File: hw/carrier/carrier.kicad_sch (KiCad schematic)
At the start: 50 parts, among them J2 PCM5102A I2S, J3 PCM5102A analog, J4 MAX4466 pigtail, J5 TP4056 OUT-/B-, J6 TP4056 B+/OUT+, J7 debug TX, J8 LiPo JST-PH, J9 TP4056 IN+ wire (J6b), Q1 DMG3415U, Q2 BC557, SW1 power SPDT 1A, SW2 MODE 6x6, U1 TL431, X1 scope X RCA pads, Y1 scope Y RCA pads

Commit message: hw+docs: apply the 2026-07-26 power-path design review
Multi-agent adversarial review of the carrier's §4 load-sharing power path
(docs/hardware/pcb-review-findings.md, added here) found the TL431 trip
point mis-derived and several safety-critical instructions wrong.  This
applies the fixes and reconciles every document that repeated them.

BOM / netlist (design.py is the source of truth; board + schematic regenerated):
  - R7 75k -> 8.2k, R8 10k, R9 2.2k -> 1k.  The old derivation dropped the
    TL431 REF bias term (I_ref*R7); with 75k it dominated and the divider
    could not reach the trip window at all.  Trip is now ~4.56 V.
  - D1 1N4148 -> BAT85 (Schottky, keeps the gate pulled low enough).
  - U1 TL431 -> TL431A (2% grade; the 1% window needs it).

Safety-critical doc corrections:
  - The JP1 escape hatch must also omit D2 -- bridging JP1 with D2 fitted
    shorts VBUS_CHG to the cell through one Schottky.  It must further omit
    R7/R8, which JP1 ties straight across the cell (231 uA with no
    comparator left to feed).  Recipe now identical in pcb.md §4.4, §4.5
    and design.py's docstring.
  - TO-92 lead-order trap documented at the netlist and in §5: onsemi
    numbers U1/Q2 1=REF,2=A,3=K, TI numbers the same package the other way
    round, and the anode is the centre lead in both -- so a TI-branded part
    drops into the footprint perfectly while sitting backwards.
  - "No USB while the battery switch is ON" is restored as a permanent rule
    until §4.4 passes on an assembled board; the review found the
    SuperMini-side threshold detection unreliable against a sagging port.

Tooling:
  - FP_OVERRIDE (11 vertical resistors) moved from gen_board.py into
    design.py so gen_schematic.py sees the same footprints; --schematic-parity
    had been flagging 11 resistors the schematic thought were horizontal.
  - route.py: new ROUTE_WIDTH_FLOOR env knob (per-net minimum track width).
    Used to measure a 14-variant VLOAD/VSW width sweep; the wider re-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
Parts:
- D1: value 1N4148 -> BAT85
- J2: symbol HY:CONN6 -> HY:X_J2
- J3: symbol HY:CONN9 -> HY:X_J3
- J4: symbol HY:CONN3 -> HY:X_J4
- J5: footprint Connector_PinSocket_2.54mm:PinSocket_1x02_P2.54mm_Vertical -> HYPEROSCI:TP4056_Pads_OUTminus_Bminus; symbol HY:CONN2 -> HY:X_J5
- J6: footprint Connector_PinSocket_2.54mm:PinSocket_1x02_P2.54mm_Vertical -> HYPEROSCI:TP4056_Pads_Bplus_OUTplus; symbol HY:CONN2 -> HY:X_J6
- J7: symbol HY:CONN2 -> HY:X_J7
- J8: symbol HY:CONN2 -> HY:X_J8
- J9: symbol HY:PAD1 -> HY:X_J9
- JA1: symbol HY:CONN8 -> HY:X_JA1
- JB1: symbol HY:CONN8 -> HY:X_JB1
- Q2: footprint Package_TO_SOT_THT:TO-92_Inline -> Package_TO_SOT_THT:TO-92_Inline_Wide
- R1, R10, R11, R12, R2, R4, R5, R6: footprint Resistor_THT:R_Axial_DIN0207_L6.3mm_D2.5mm_P10.16mm_Horizontal -> Resistor_THT:R_Axial_DIN0207_L6.3mm_D2.5mm_P2.54mm_Vertical
- R7: value 82k 1% -> 8.2k 1%; footprint Resistor_THT:R_Axial_DIN0207_L6.3mm_D2.5mm_P10.16mm_Horizontal -> Resistor_THT:R_Axial_DIN0207_L6.3mm_D2.5mm_P2.54mm_Vertical
- R8: value 100k 1% -> 10k 1%; footprint Resistor_THT:R_Axial_DIN0207_L6.3mm_D2.5mm_P10.16mm_Horizontal -> Resistor_THT:R_Axial_DIN0207_L6.3mm_D2.5mm_P2.54mm_Vertical
- R9: value 2.2k -> 1k; footprint Resistor_THT:R_Axial_DIN0207_L6.3mm_D2.5mm_P10.16mm_Horizontal -> Resistor_THT:R_Axial_DIN0207_L6.3mm_D2.5mm_P2.54mm_Vertical
- U1: value TL431 -> TL431A; footprint Package_TO_SOT_THT:TO-92_Inline -> Package_TO_SOT_THT:TO-92_Inline_Wide
- X1: symbol HY:CONN2 -> HY:X_X1
- Y1: symbol HY:CONN2 -> HY:X_Y1
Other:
- note added: "!! B− must NOT join GND (protection is low-side)"
- note added: "!! state 4 (SuperMini USB + SW1 ON + battery): the trip is unreachable from battery mode — Q1 stays on and the port back-feeds the cell. RULE 1 stands until pcb.md §4.4 passes on an assembled carrier: SW1 OFF before ANY USB."
- note added: "4 units for the show · 70 × 50 mm 2-layer · modules socketed · ESP32-C3 SuperMini + PCM5102A + TP4056 + MAX4466"
- note added: "BATTERY + CHARGER"
- note added: "BREADBOARD DELTA (wiring.md): no load-share block — OUT+ → switch → 5V pin direct. VBAT_RAW = BAT_PLUS, VBAT_SW ≈ VLOAD. All signal wiring is identical."
- note added: "CONTROLS + LEDs"
- note added: "CSM4056T + DW01 + FS8205 (protected) charge on its own USB-C only — RULE 2: charge with SW1 OFF"
- note added: "CW = higher cutoff"
- note added: "D3: DNP naive-OR experiment — do not fit (§4.1)"
- note added: "EEMB LP103454 2000 mAh LiPo (cell off-board — polarity silk!)"
- note added: "ESP32-C3 SUPERMINI (socketed, antenna → west edge)"
- note added: "GENERATED FILE — drawn by tools/gen_schematic.py from tools/design.py (the netlist source of truth). Never edit by hand: edit design.py, regenerate, re-run the gates (check_netlist.py, ERC, DRC --schematic-parity)."
- note added: "GPIO2 strap: high at reset, nothing else on it"
- note added: "GPIO8/9: onboard, NC"
- note added: "GY-PCM5102A (socketed, purple)"
- note added: "HYPEROSCI SLAVE UNIT — CARRIER v1.1 WIRING DIAGRAM"
- note added: "I2S DAC + SCOPE OUT"
- note added: "J3 FMT/XSMT/DEMP/FLT are set by the module's own back bridges: FLT=L DEMP=L XSMT=H FMT=L — solder BEFORE first power-up; XSMT open = DAC hard-muted (#1 no-output cause — wiring.md §4)"
- note added: "JP1 — plan-A escape hatch: bridge, omit Q1 Q2 U1 D1 D2 + R7 R8"
- note added: "LOAD-SHARING POWER PATH — carrier only, not on the breadboard (pcb.md §4)"
- note added: "M3 holes — GND ring, fence-stitched (§6.2)"
- note added: "MIC INPUT"
- note added: "R10/R11: fit 0 Ω if the module's ~470 Ω output R is confirmed in-line (§3.2) X/Y ground pads + J3 AGND = analog island, single-neck join near J2 GND (§6.3)"
- note added: "READ ME — BUILD + SAFETY"
- note added: "RULE 1 — SW1 OFF before plugging ANY USB. The load-share block was meant to retire this rule; the 2026-07-26 review shows it cannot (state 4, §4.1/§4.3). The rule stays until §4.4 passes on an assembled board."
- note added: "RULE 2 — charge with SW1 OFF (TP4056 cannot terminate into a load)."
- note added: "RULE 3 — one USB at a time: charger-USB = charging, module-USB = development, SW1 ON only with no USB."
- note added: "SCK → GND on the carrier: DAC clocks itself by PLL from BCK (§3.2)"
- note added: "SHOW BUILD (plan A, §4.5): bridge JP1 and DO NOT FIT Q1, Q2, U1, D1, D2, R7, R8. Never leave D2 fitted on a JP1-bridged board — the charger's USB would land on the cell raw, upstream of the switch."
- note added: "SW1 downstream of Q1: VSW live in BOTH positions (state 6)"
- note added: "TEST + MECH"
- note added: "TO-92 LEAD ORDER (U1, Q2): vendors number the same package opposite ways (TL431 onsemi vs TI; BC557 C-B-E vs E-B-C) — check the datasheet of the part actually bought (pcb.md §5)."
- note added: "TP1 VBUS_CHG · TP2 VSW · TP3 GATE · TP5 VBAT_SENSE"
- note added: "TP4056 USB-C charger module (socketed)"
- note added: "UART0 TX log header"
- note added: "WiFi burst reservoir"
- note added: "always-on: ~21 µA; /2 → GPIO1"
- note added: "at J2 VIN"
- note added: "at mic socket (AGND island)"
- note added: "body diode D→S: VSW bootstraps in battery mode (state 1)"
- note added: "internal pull-up + 30 ms debounce (config.h)"
- note added: "module USB-C = flash / debug / console ONLY. !! RULE 1: SW1 OFF before plugging — VBUS ties straight to the 5V pin (meter-confirmed). clone silk may print RX/TX = GPIO20/GPIO21. 3V3 pin = module LDO out — powers everything else."
- note added: "trip ≈ 4.56 V typ (4.46–4.66 V @ 25 °C) 8.2k/10k 1 % + TL431A — populate-time choice, see pcb.md §4.2 divider table"
- note added: "~0.5 mA per LED — dim by design (battery)"
- note added: "→ MAX4466 on ~10 cm 3-wire pigtail (off-board), capsule exits the enclosure, aimed at the PA; gain trimmer mid-travel to start"
- note added: "→ solder ~50 cm RCA leads: X → scope CH1, Y → CH2 XY mode, DC-coupled, 1 MΩ (never 50 Ω) ±3 V full-scale per axis, ground-centred"
- note removed: "Battery + TP4056"
- note removed: "Mic + controls"
- note removed: "PCM5102A + scope out"
- note removed: "Power path"
- note removed: "SuperMini socket"
- note removed: "Test + mech"
- title: HYPEROSCI carrier v1.0 -> HYPEROSCI carrier v1.1 — wiring diagram
- moved on the sheet: RV1, SW2, U1

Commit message: hw/carrier: RV1 was the wrong part's footprint — corrected, re-routed
The RV097NS 5-pin is "mono WITH SWITCH", right-angle.  RV097NS_Vertical
drew it as a vertical pot with two mechanical bracket lugs: row 2 as oval
slots 9.5 mm apart and 7.0 mm behind the pot row, taken "from the common
RV09 drawing" and flagged unverified since the first commit.  The real
part has no bracket lugs at all.  Row 2 is a plain SPST on 1.0 mm holes
5.0 mm apart and 6.25 mm behind, and the mounting surface sits 5.0 mm in
FRONT of the pot row, not 1.2 mm.  Every row-2 pad was 2.25 mm out in X
and 0.75 mm in Y.  The part would not have gone into the board.

Settled by the seller's mechanical drawing, which agrees to the decimal
with KiCad's stock Potentiometer_Alps_RK097_Single_Horizontal_Switch
(from ALPS rk097.pdf) -- and independently by its 9.5 x 11.35 mm
cross-section matching the 2026-07-18 calipers' 9.5 x 11.3.

  - footprint renamed RV097NS_Vertical -> RV097NS_Horizontal_Switch; body
    9.5 x 13.0, bushing and 15 mm shaft on F.Fab, silk open on the
    mounting face because that face lands on Edge.Cuts.
  - RV1's Y stopped being a free parameter: 45.0 puts the mounting
    surface exactly on the board's south edge (y=50), so the M7x0.75
    bushing and shaft hang off it and through the enclosure wall.
  - pads 4/5 stay on GND, deliberately.  No safe spare GPIO exists
    (GPIO0 is MIC_OUT; GPIO8/9 are strapping pins that must be high at
    reset and this switch makes at one end of rotation; GPIO21 is the
    console UART TX, an output), and with no bracket lugs those two
    0.8 mm pins in the pour are the part's only rear anchoring against a
    bare shaft turned by hand.  Symbol says S1/S2 now, not LUG.

Two things broke on the way, both fixed in the generators:

  - ROUTE_SEED 77 stopped working.  Moving five pads was enough: phase D
    ended STUCK with 3 unbridgeable pour clusters and DRC reported 2
    unconnected GND_main islands.  A 24-variant sweep (6 seeds x 4 halo
    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
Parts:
- RV1: value RV097NS B10K -> RV097NS B10K +SW; footprint HYPEROSCI:RV097NS_Vertical -> HYPEROSCI:RV097NS_Horizontal_Switch
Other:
- note added: "both ends on GND (see design.py)"
- note added: "pins 4/5 = end-of-travel SPST, unused:"
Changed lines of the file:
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@@
     (exclude_from_sim no) (in_bom yes) (on_board yes) (dnp no)
     (property "Reference" "RV1" (at 118.11 160.02 0) (effects (font (size 1.27 1.27)) (justify left)))
-    (property "Value" "RV097NS B10K" (at 137.16 162.56 0) (effects (font (size 1.02 1.02)) (justify left)))
-    (property "Footprint" "HYPEROSCI:RV097NS_Vertical" (at 132.08 165.1 0) (effects (font (size 1.27 1.27)) (hide yes)))
+    (property "Value" "RV097NS B10K +SW" (at 137.16 162.56 0) (effects (font (size 1.02 1.02)) (justify left)))
+    (property "Footprint" "HYPEROSCI:RV097NS_Horizontal_Switch" (at 132.08 165.1 0) (effects (font (size 1.27 1.27)) (hide yes)))
     (property "Datasheet" "" (at 132.08 165.1 0) (effects (font (size 1.27 1.27)) (hide yes)))
     (pin "1")
@@
   (text "CONTROLS + LEDs" (exclude_from_sim no) (at 113.03 142.875 0) (effects (font (size 1.6 1.6) (bold yes)) (justify left)))
   (text "CW = higher cutoff" (exclude_from_sim no) (at 139.7 171.45 0) (effects (font (size 0.9 0.9)) (justify left)))
+  (text "pins 4/5 = end-of-travel SPST, unused:" (exclude_from_sim no) (at 114.3 175.895 0) (effects (font (size 0.9 0.9)) (justify left)))
+  (text "both ends on GND (see design.py)" (exclude_from_sim no) (at 114.3 178.435 0) (effects (font (size 0.9 0.9)) (justify left)))
   (text "internal pull-up + 30 ms debounce (config.h)" (exclude_from_sim no) (at 114.3 196.215 0) (effects (font (size 0.9 0.9)) (justify left)))
   (text "GPIO2 strap:\nhigh at reset,\nnothing else on it" (exclude_from_sim no) (at 168.91 153.67 0) (effects (font (size 0.9 0.9)) (justify left)))

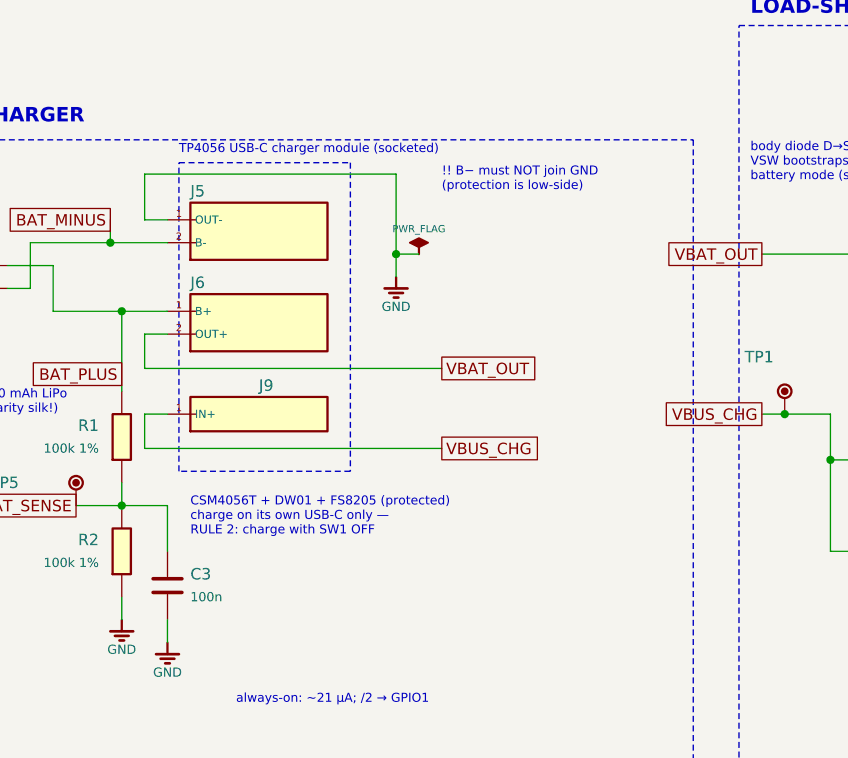
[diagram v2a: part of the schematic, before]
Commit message: hw/carrier: the TP4056 was a 21.65 mm cantilever — second mount row added
J5/J6 put all four pins in ONE column at one end of the module, and the
USB-C jack is at the other.  A row of pins resists rotation about its own
axis only by bending, so the charge port sat on a diving board:

  0.64 mm square pin, ~5 mm free length -> EI/L = 0.061 N*m/rad each
  four of them, all on the axis         -> ~0.25 N*m/rad total
  5 N off-axis nudge on the plug        -> 0.11 N*m -> ~25 deg

Crude (a machined socket grips several mm of barrel, so reality is
stiffer), but the order of magnitude is the point: grams of side load,
tens of degrees, on the one connector handled every charge cycle at
10-20 N of insertion force.

The module already carried the fix.  Two ~2.8 mm bare-copper pads on
1.68 mm plated holes sit at its USB-C-end corners, in line with OUT+
("+" silk, next to R8) and OUT-.  The carrier already had a pad on one
of them -- J9, drawn as a wire pad for the IN+ sense tap.  So:

  - J9 became a machined socket and moved 0.65 mm west onto the real
    hole.  That also deletes the one hand-soldered wire in the power
    path, which in 4.3 state 2 carries the WHOLE board load (~150 mA
    average, ~350 mA WiFi bursts, ~4 A/<100 us C1 inrush), not a sense
    current.
  - J10 was added on the other corner, ON NO NET.  pcb.md 2 asserts
    TP4056 IN- is the same copper as OUT- and that is the usual
    protected topology, but it has never been ohmed on this module --
    and if it is wrong, bonding it to carrier GND shorts across the
    DW01/FS8205 and the cell loses its protection.  A floating pin
    anchors the far end just as well, so the question stays open.
  - WirePad_D1.0 -> TP4056_MountPin (same 1.0 mm drill / 2.2 mm pad; the
    name and the docstring were the only wrong parts).
  - BOM: six machined single-pin sockets per board, not four.

Why the offset is a caliper number overriding the photogrammetry, which
is the only place in measured.py that happens.  The pi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
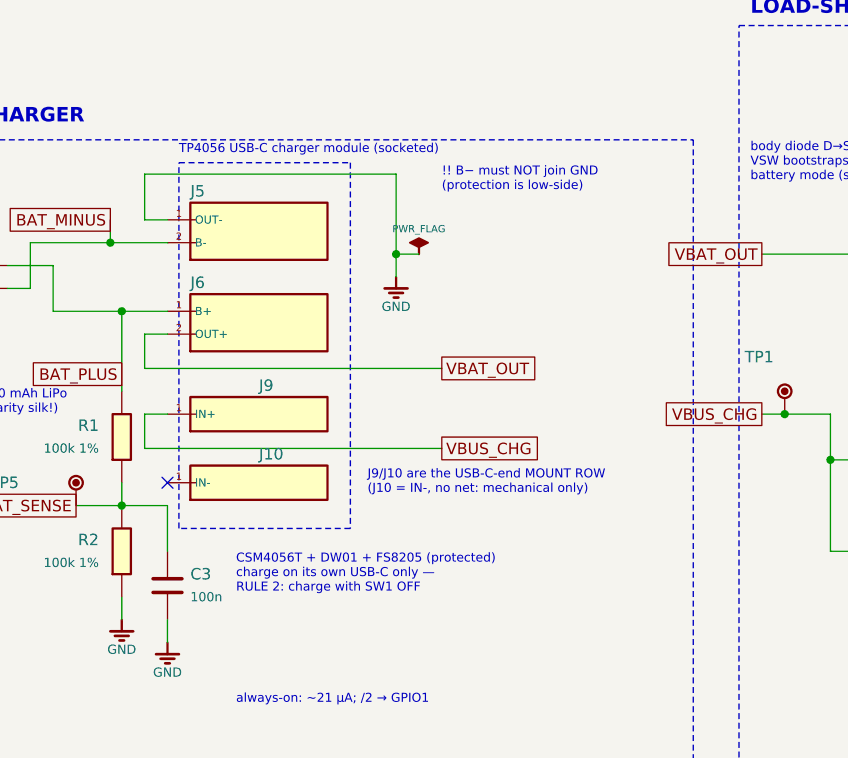
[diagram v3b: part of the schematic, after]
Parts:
- added J10: TP4056 IN- / mount, HYPEROSCI:TP4056_MountPin, symbol HY:X_J10
- J9: value TP4056 IN+ wire (J6b) -> TP4056 IN+ / mount (J6b); footprint HYPEROSCI:WirePad_D1.0 -> HYPEROSCI:TP4056_MountPin
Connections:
- no-connect marks 8 -> 9
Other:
- note added: "J9/J10 are the USB-C-end MOUNT ROW (J10 = IN-, no net: mechanical only)"
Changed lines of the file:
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@@
     (exclude_from_sim no) (in_bom yes) (on_board yes) (dnp no)
     (property "Reference" "J9" (at 58.42 60.325 0) (effects (font (size 1.27 1.27)) (justify left)))
-    (property "Value" "TP4056 IN+ wire (J6b)" (at 55.88 63.5 0) (effects (font (size 1.27 1.27)) (hide yes)))
-    (property "Footprint" "HYPEROSCI:WirePad_D1.0" (at 55.88 63.5 0) (effects (font (size 1.27 1.27)) (hide yes)))
+    (property "Value" "TP4056 IN+ / mount (J6b)" (at 55.88 63.5 0) (effects (font (size 1.27 1.27)) (hide yes)))
+    (property "Footprint" "HYPEROSCI:TP4056_MountPin" (at 55.88 63.5 0) (effects (font (size 1.27 1.27)) (hide yes)))
     (property "Datasheet" "" (at 55.88 63.5 0) (effects (font (size 1.27 1.27)) (hide yes)))
     (pin "1")
     (instances (project "carrier" (path "/df23c651-dbe4-5734-8eb8-65605c7cfe14" (reference "J9") (unit 1))))
+  )
+  (symbol (lib_id "HY:X_J10") (at 55.88 71.12 0) (unit 1)
+    (exclude_from_sim no) (in_bom yes) (on_board yes) (dnp no)
+    (property "Reference" "J10" (at 58.42 67.945 0) (effects (font (size 1.27 1.27)) (justify left)))
+    (property "Value" "TP4056 IN- / mount" (at 55.88 71.12 0) (effects (font (size 1.27 1.27)) (hide yes)))
+    (property "Footprint" "HYPEROSCI:TP4056_MountPin" (at 55.88 71.12 0) (effects (font (size 1.27 1.27)) (hide yes)))
+    (property "Datasheet" "" (at 55.88 71.12 0) (effects (font (size 1.27 1.27)) (hide yes)))
+    (pin "1")
+    (instances (project "carrier" (path "/df23c651-dbe4-5734-8eb8-65605c7cfe14" (reference "J10") (unit 1))))
   )
   (symbol (lib_id "HY:X_J7") (at 147.32 205.74 0) (unit 1)
@@
   (no_connect (at 297.18 170.18))
   (no_connect (at 297.18 172.72))
+  (no_connect (at 48.26 71.12))
   (no_connect (at 238.76 50.8))
   (global_label "BAT_PLUS" (shape passive) (at 43.18 59.055 180) (fields_autoplaced yes) (effects (font (size 1.27 1.27)) (justify right)))
@@
   (text "BATTERY + CHARGER" (exclude_from_sim no) (at 12.7 30.48 0) (effects (font (size 1.6 1.6) (bold yes)) (justify left)))
   (text "TP4056 USB-C charger module (socketed)" (exclude_from_sim no) (at 49.53 34.163 0) (effects (font (size 1.0 1.0)) (justify left)))
-  (text "CSM4056T + DW01 + FS8205 (protected)\ncharge on its own USB-C only —\nRULE 2: charge with SW1 OFF" (exclude_from_sim no) (at 50.8 74.93 0) (effects (font (size 1.0 1.0)) (justify left)))
+  (text "J9/J10 are the USB-C-end MOUNT ROW\n(J10 = IN-, no net: mechanical only)" (exclude_from_sim no) (at 70.485 71.12 0) (effects (font (size 1.0 1.0)) (justify left)))
+  (text "CSM4056T + DW01 + FS8205 (protected)\ncharge on its own USB-C only —\nRULE 2: charge with SW1 OFF" (exclude_from_sim no) (at 55.88 81.28 0) (effects (font (size 1.0 1.0)) (justify left)))
   (text "EEMB LP103454 2000 mAh LiPo\n(cell off-board — polarity silk!)" (exclude_from_sim no) (at 15.24 62.23 0) (effects (font (size 1.0 1.0)) (justify left)))
   (text "!! B− must NOT join GND\n(protection is low-side)" (exclude_from_sim no) (at 78.74 37.465 0) (effects (font (size 1.0 1.0)) (justify left)))
@@
   (text "4 units for the show · 70 × 50 mm 2-layer · modules socketed · ESP32-C3 SuperMini + PCM5102A + TP4056 + MAX4466" (exclude_from_sim no) (at 11.43 16.129 0) (effects (font (size 1.1 1.1)) (justify left)))
   (polyline (pts (xy 11.43 33.02) (xy 106.68 33.02) (xy 106.68 127) (xy 11.43 127) (xy 11.43 33.02)) (stroke (width 0.1524) (type dash)))
-  (polyline (pts (xy 49.53 35.56) (xy 68.58 35.56) (xy 68.58 69.85) (xy 49.53 69.85) (xy 49.53 35.56)) (stroke (width 0.1524) (type dash)))
+  (polyline (pts (xy 49.53 35.56) (xy 68.58 35.56) (xy 68.58 76.2) (xy 49.53 76.2) (xy 49.53 35.56)) (stroke (width 0.1524) (type dash)))
   (polyline (pts (xy 111.76 20.32) (xy 299.72 20.32) (xy 299.72 121.92) (xy 111.76 121.92) (xy 111.76 20.32)) (stroke (width 0.1524) (type dash)))
   (polyline (pts (xy 304.8 33.02) (xy 406.4 33.02) (xy 406.4 91.44) (xy 304.8 91.44) (xy 304.8 33.02)) (stroke (width 0.1524) (type dash)))
